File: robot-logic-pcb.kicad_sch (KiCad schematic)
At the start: 21 parts, among them U1 NRF24L01_Breakout

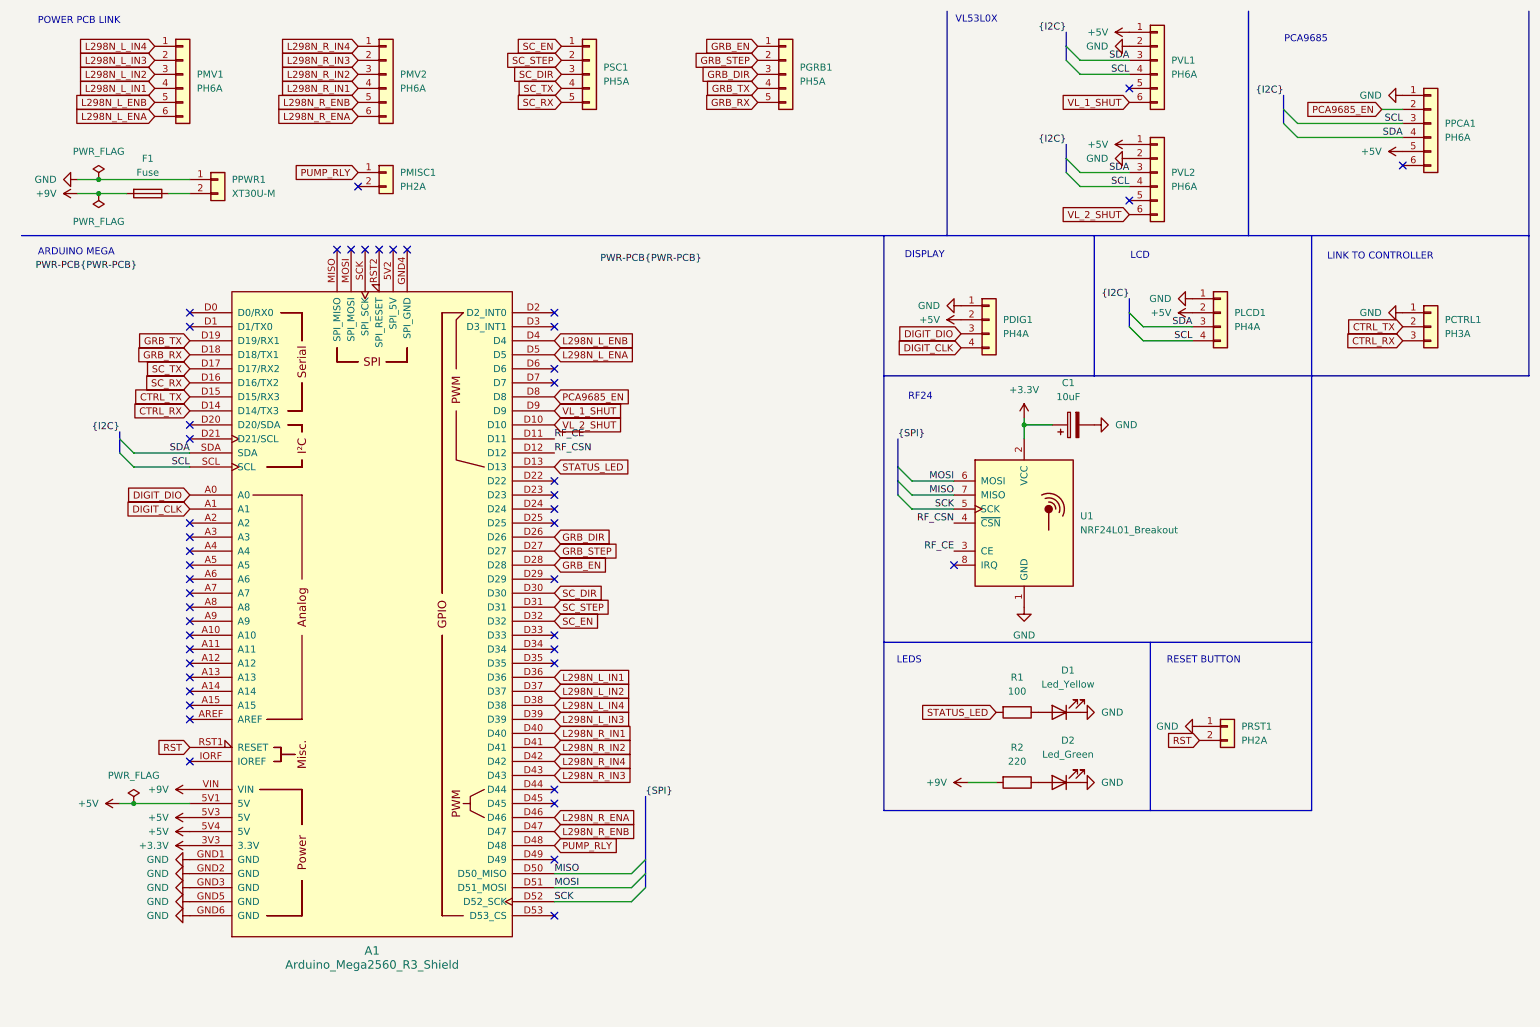
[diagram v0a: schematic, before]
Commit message: Post regionales Adds ESP32 for steppers and diodes to protect MCUs
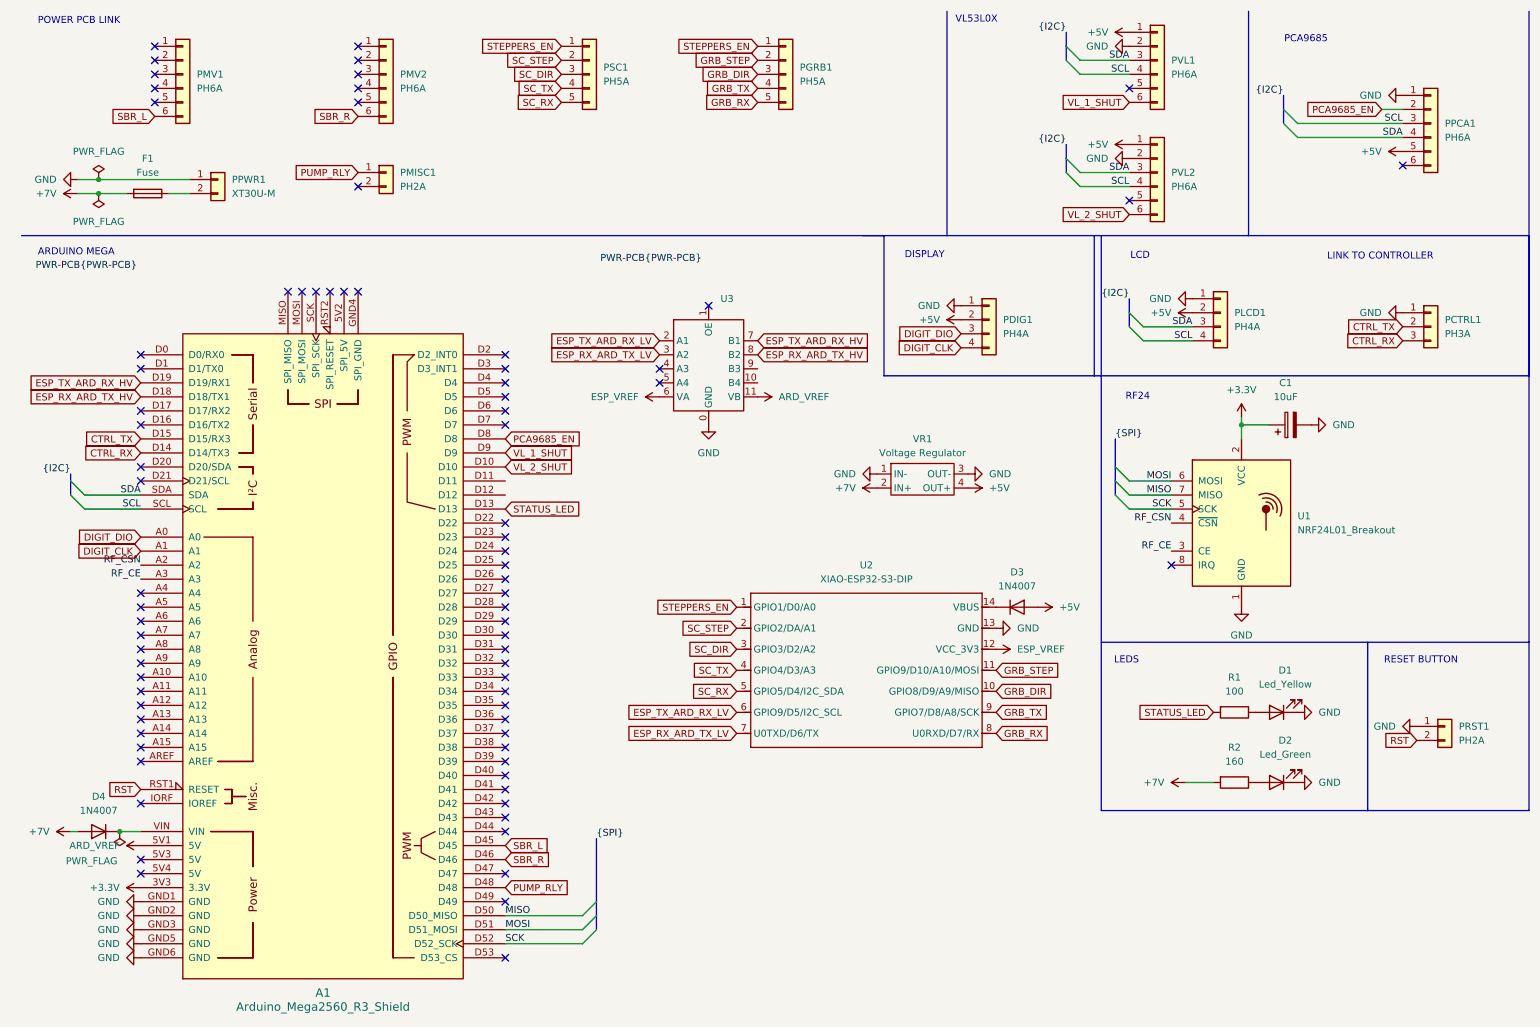
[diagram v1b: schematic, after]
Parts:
- added D3, D4: 1N4007, Diode_THT:D_DO-41_SOD81_P2.54mm_Vertical_AnodeUp, symbol Device:D
- added U2: XIAO-ESP32-S3-DIP, Project:XIAO-ESP32S3-DIP, symbol Seeed_Studio_XIAO_Series:XIAO-ESP32-S3-DIP
- added U3: ~, Project:TXB0104-BREAKOUT, symbol Project:TXB0104-BREAKOUT
- added VR1: Voltage Regulator, Project:MP1584EN, symbol Project:Voltage_Regulator_Module
- R2: value 220 -> 160
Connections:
- net +5V: now also D3.2 (A), VR1.4 (OUT+); no longer A1.5V1 (5V), A1.5V3 (5V), A1.5V4 (5V)
- net GND: now also U2.13 (GND), U3.0 (GND), VR1.1 (IN-), VR1.3 (OUT-)
- net GRB_DIR: now also U2.10 (GPIO8/D9/A9/MISO); no longer A1.D26
- net GRB_RX: now also U2.8 (U0RXD/D7/RX); no longer A1.D18 (D18/TX1)
- net GRB_STEP: now also U2.11 (GPIO9/D10/A10/MOSI); no longer A1.D27
- net GRB_TX: now also U2.9 (GPIO7/D8/A8/SCK); no longer A1.D19 (D19/RX1)
- net RF_CE: now also A1.A3; no longer A1.D11
- net RF_CSN: now also A1.A2; no longer A1.D12
- net SC_DIR: now also U2.3 (GPIO3/D2/A2); no longer A1.D30
- net SC_RX: now also U2.5 (GPIO5/D4/I2C_SDA); no longer A1.D16 (D16/TX2)
- net SC_STEP: now also U2.2 (GPIO2/DA/A1); no longer A1.D31
- net SC_TX: now also U2.4 (GPIO4/D3/A3); no longer A1.D17 (D17/RX2)
- net SBR_L: now reaches A1.D45
- net SBR_L: now also PMV1.6 (Pin_6)
- net +9V renamed +7V
- net +7V: now also D4.2 (A), VR1.2 (IN+); no longer A1.VIN
- net GRB_EN: no longer names the net of A1.D28
- net GRB_EN: no longer PGRB1.1 (Pin_1)
- net L298N_L_ENA: no longer names the net of A1.D5
- net L298N_L_ENA: no longer PMV1.6 (Pin_6)
- net L298N_L_ENB: no longer names the net of A1.D4
- net L298N_L_ENB: no longer PMV1.5 (Pin_5)
- net L298N_L_IN1: no longer names the net of A1.D36
- net L298N_L_IN1: no longer PMV1.4 (Pin_4)
- net L298N_L_IN2: no longer names the net of A1.D37
- net L298N_L_IN2: no longer PMV1.3 (Pin_3)
- net L298N_L_IN3: no longer names the net of A1.D39
- net L298N_L_IN3: no longer PMV1.2 (Pin_2)
- net L298N_L_IN4: no longer names the net of A1.D38
- net L298N_L_IN4: no longer PMV1.1 (Pin_1)
- net L298N_R_ENA renamed SBR_R
- net L298N_R_ENB: no longer names the net of PMV2.5 (Pin_5)
- net L298N_R_ENB: no longer A1.D47
- net L298N_R_IN1: no longer names the net of PMV2.4 (Pin_4)
- net L298N_R_IN1: no longer A1.D40
- net L298N_R_IN2: no longer names the net of PMV2.3 (Pin_3)
- net L298N_R_IN2: no longer A1.D41
- net L298N_R_IN3: no longer names the net of PMV2.2 (Pin_2)
- net L298N_R_IN3: no longer A1.D43
- net L298N_R_IN4: no longer names the net of PMV2.1 (Pin_1)
- net L298N_R_IN4: no longer A1.D42
- net SC_EN: no longer names the net of A1.D32
- net SC_EN: no longer PSC1.1 (Pin_1)
- new net: D3.1 (K), U2.14 (VBUS)
- new net: A1.VIN, D4.1 (K)
- new net ARD_VREF: A1.5V1 (5V), U3.11 (VB)
- new net ESP_RX_ARD_TX_HV: A1.D18 (D18/TX1), U3.8 (B2)
- new net ESP_RX_ARD_TX_LV: U2.7 (U0TXD/D6/TX), U3.3 (A2)
- new net ESP_TX_ARD_RX_HV: A1.D19 (D19/RX1), U3.7 (B1)
- new net ESP_TX_ARD_RX_LV: U2.6 (GPIO9/D5/I2C_SCL), U3.2 (A1)
- new net ESP_VREF: U2.12 (VCC_3V3), U3.6 (VA)
- new net STEPPERS_EN: PGRB1.1 (Pin_1), PSC1.1 (Pin_1), U2.1 (GPIO1/D0/A0)
- no-connect marks 47 -> 78
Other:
- moved on the sheet: A1, C1, D1, D2, PRST1, R1, R2, U1

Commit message: forgot to save sch lol
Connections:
- net PCA9685_EN: now also A1.D4; no longer A1.D8
- no-connect marks 78 -> 80
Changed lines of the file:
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@@
+	)
+	(no_connect
+		(at 99.06 90.17)
 	)
 	(no_connect
@@
 	)
 	(no_connect
+		(at 99.06 97.79)
+	)
+	(no_connect
 		(at 33.02 166.37)
 	)
@@
 	)
 	(no_connect
-		(at 99.06 80.01)
-	)
-	(no_connect
 		(at 62.23 63.5)
 	)
@@
 	(no_connect
 		(at 72.39 63.5)
+	)
+	(no_connect
+		(at 99.06 100.33)
 	)
 	(no_connect
@@
 		)
 	)
+	(global_label "PCA9685_EN"
+		(shape input)
+		(at 99.06 80.01 0)
+		(fields_autoplaced yes)
+		(effects
+			(font
+				(size 1.27 1.27)
+			)
+			(justify left)
+		)
+		(property "Intersheetrefs" "${INTERSHEET_REFS}"
+			(at 113.9589 80.01 0)
+			(effects
+				(font
+					(size 1.27 1.27)
+				)
+				(justify left)
+				(hide yes)
+			)
+		)
+	)
 	(global_label "SC_STEP"
 		(shape input)
@@
 				(hide yes)
 			)
-		)
-	)
-	(global_label "PCA9685_EN"
-		(shape input)
-		(at 99.06 90.17 0)
-		(fields_autoplaced yes)
-		(effects
-			(font
-				(size 1.27 1.27)
-			)
-			(justify left)
-		)
-		(property "Intersheetrefs" "${INTERSHEET_REFS}"
-			(at 113.9589 90.17 0)
-			(effects
-				(font
-					(size 1.27 1.27)
-				)
-				(justify left)
-				(hide yes)
-			)
